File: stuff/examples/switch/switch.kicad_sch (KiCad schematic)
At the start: 3 parts

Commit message: - some fixme
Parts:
- added DEC1, DEC2: decode_3_bit, symbol chip:DECODE_3BIT
- added Led1, Led2, Led3, Led4: ~, symbol chip:LED
- added SA2, SA3: SW_Push, symbol Switch:SW_Push
- added pulldown1, pulldown2: pull_down, symbol chip:PULLDOWN
- added pullup1: pull_up, symbol chip:PULLUP
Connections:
- net gnd: now also DEC2.12 (~{CS}), DEC2.3 (A2)
- net at SA1.2, pullup2.1 (OUT): now also DEC1.12 (~{CS}); no longer Led5.1 (IN)
- new net: DEC2.5 (Q1), Led2.1 (IN)
- new net: DEC1.2 (A1), DEC1.3 (A2), DEC2.1 (A0), Led5.1 (IN), SA2.1, SA3.2, pulldown1.1 (OUT)
- new net: DEC1.1 (A0), pullup1.1 (OUT)
- new net: DEC1.5 (Q1), DEC2.2 (A1), pulldown2.1 (OUT)
- new net: DEC2.4 (Q0), Led1.1 (IN)
- new net: DEC2.6 (Q2), Led3.1 (IN)
- new net: DEC2.7 (Q3), Led4.1 (IN)
- new net: DEC1.4 (Q0), SA3.1
- new net pwr: SA2.2
- no-connect marks 0 -> 10
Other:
- moved on the sheet: Led5

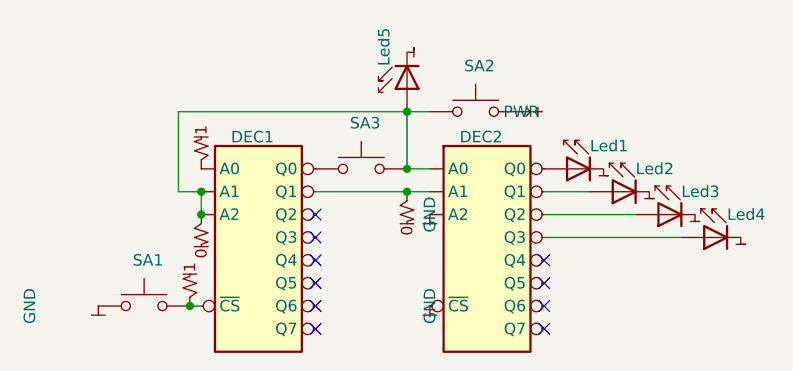
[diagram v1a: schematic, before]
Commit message: cleanup BusInterconnect optimise fix generated Class Name fix
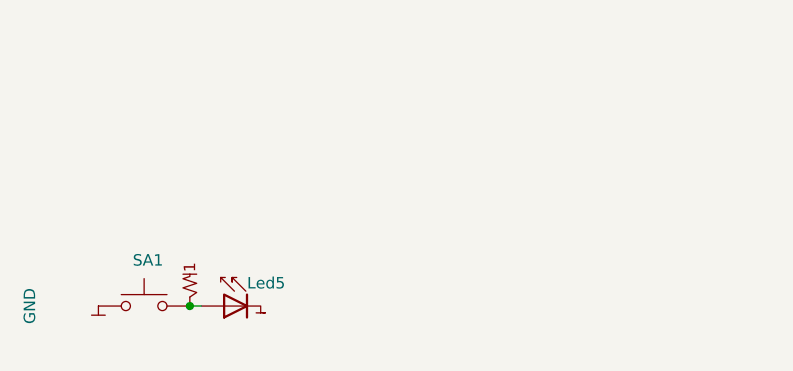
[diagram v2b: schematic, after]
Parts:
- removed DEC1, DEC2: decode_3_bit, symbol chip:DECODE_3BIT
- removed Led1, Led2, Led3, Led4: ~, symbol chip:LED
- removed SA2, SA3: SW_Push, symbol Switch:SW_Push
- removed pulldown1, pulldown2: pull_down, symbol chip:PULLDOWN
- removed pullup1: pull_up, symbol chip:PULLUP
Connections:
- net at Led5.1 (IN): now also SA1.2, pullup2.1 (OUT)
- no-connect marks 10 -> 0
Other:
- moved on the sheet: Led5
